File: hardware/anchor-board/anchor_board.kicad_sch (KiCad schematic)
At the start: 54 parts, among them J1 USB4105-GF-A, SW1 SKHHALA010, U1 DWM3001C, U2 TPD2E2U06, U3 BQ24074, U4 DW01A, U5 FS8205A, U6 TLV75530, U7 W25Q128JVSIQ, U8 TPS22916C

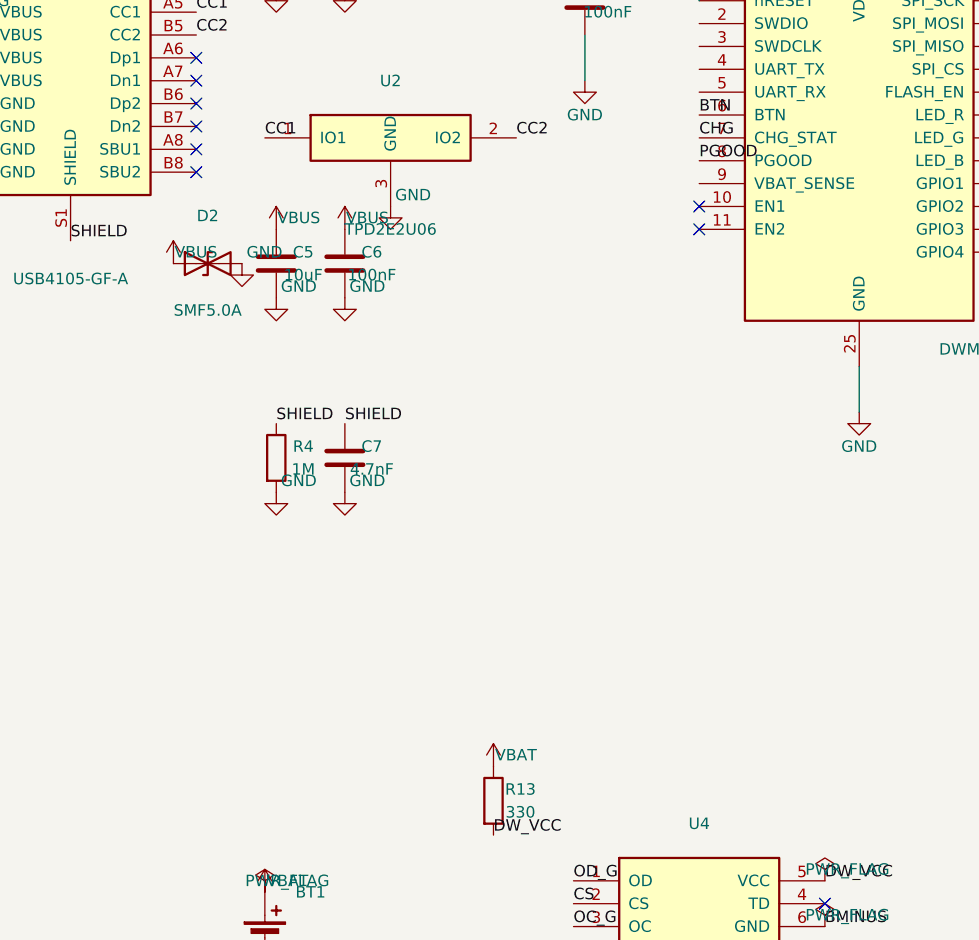
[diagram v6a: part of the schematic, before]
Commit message: Capture §4.8 VBAT voltage sense divider on anchor-board schematic
Adds R22/R23 (1M+1M high-impedance divider) from VBAT with C19 100nF
filter cap, tap driving U1 VBAT_SENSE (pin 9) for the hub's battery_pct
BLE field. ERC 21 -> 19 (remaining errors are §4.9 dev-rail pins).
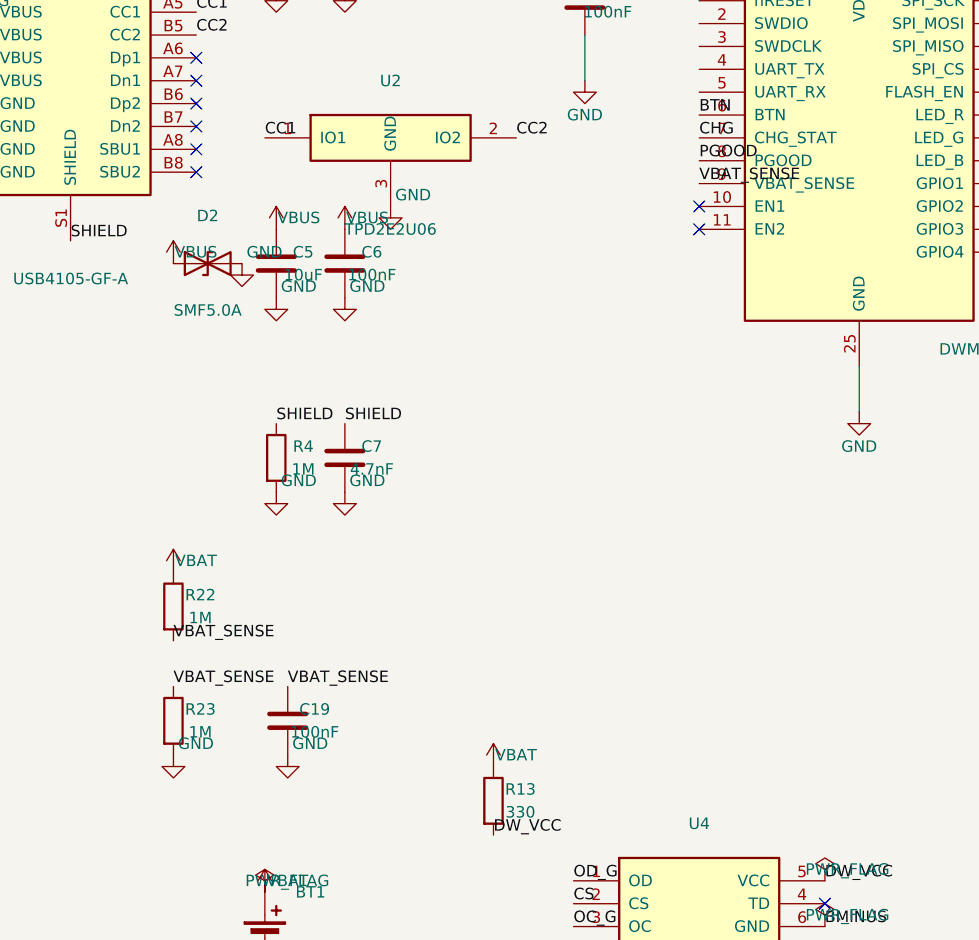
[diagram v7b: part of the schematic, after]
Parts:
- added C19: 100nF, Capacitor_SMD:C_0402_1005Metric, symbol Device:C
- added R22, R23: 1M, Resistor_SMD:R_0402_1005Metric, symbol Device:R
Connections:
- net GND: now also C19.2, R23.2
- net VBAT: now also R22.1
- net VBAT_SENSE: now reaches U1.9 (VBAT_SENSE)
- net VBAT_SENSE: now also C19.1, R22.2, R23.1

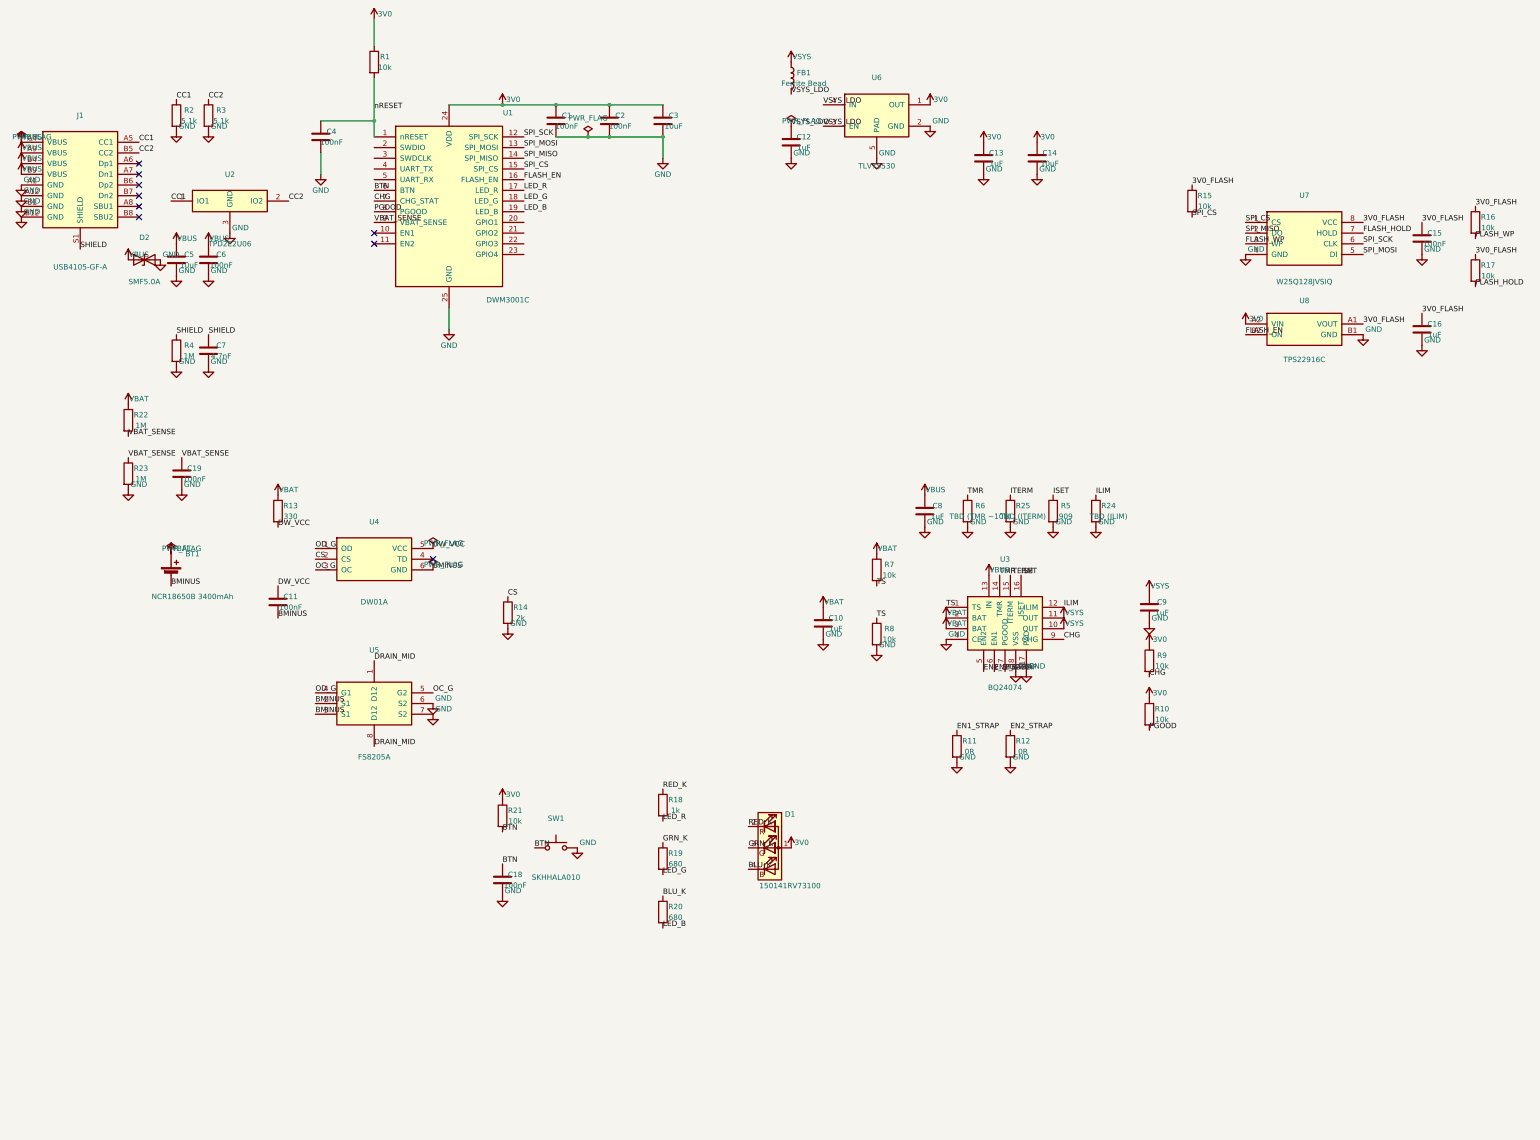
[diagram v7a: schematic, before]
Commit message: Capture §4.9 rail test points + §7 break-off dev rail — schematic ERC-clean
Completes the anchor-board schematic:
- §4.9: TP1-TP6 (VBUS/VSYS/VBAT/3V0/GND x2) + C20 10uF 3V0 bulk cap
- §7 dev rail: J2 2x5 SWD header, J8 Tag-Connect TC2030 pads, J3 UART
  header, J4 GPIO breakout, J5 3V0 current-shunt jumper (+ R26 0R
  production replacement), J6 LED-disable jumper, J7 reset/boot pads
- LDO output split into 3V0_LDO -> (shunt jumper / 0R) -> 3V0 so the
  sleep-current meter sees true load current; LED anode on LED_VCC
  behind the disable jumper
- DWM3001C SWDCLK/UART_RX pins -> passive (driven by external tooling)

ERC: 0 errors, 10 warnings (all footprint-not-found placeholders for
custom parts, resolved at layout).
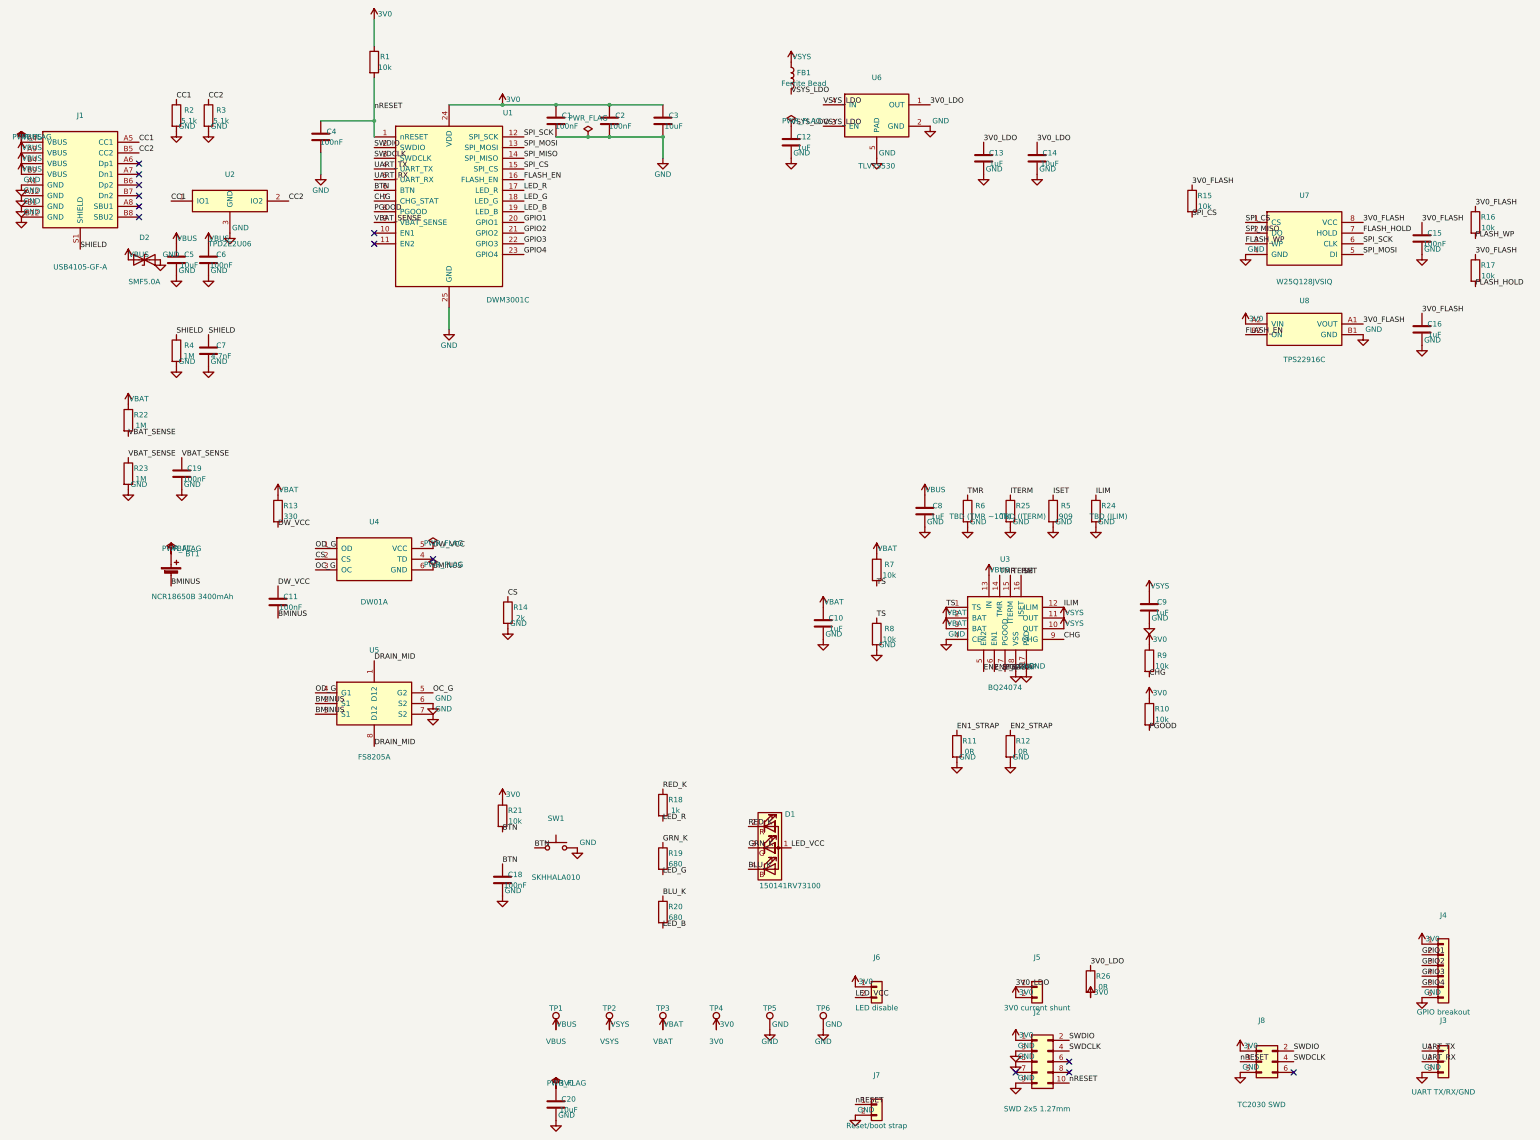
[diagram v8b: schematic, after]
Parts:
- added C20: 10uF, Capacitor_SMD:C_0805_2012Metric, symbol Device:C
- added J2: SWD 2x5 1.27mm, Connector_PinHeader_1.27mm:PinHeader_2x05_P1.27mm_Vertical, symbol Connector_Generic:Conn_02x05_Odd_Even
- added J3: UART TX/RX/GND, Connector_PinHeader_2.54mm:PinHeader_1x03_P2.54mm_Vertical, symbol Connector_Generic:Conn_01x03
- added J4: GPIO breakout, Connector_PinHeader_2.54mm:PinHeader_1x06_P2.54mm_Vertical, symbol Connector_Generic:Conn_01x06
- added J5: 3V0 current shunt, Connector_PinHeader_2.54mm:PinHeader_1x02_P2.54mm_Vertical, symbol Connector_Generic:Conn_01x02
- added J6: LED disable, Connector_PinHeader_2.54mm:PinHeader_1x02_P2.54mm_Vertical, symbol Connector_Generic:Conn_01x02
- added J7: Reset/boot strap, Connector_PinHeader_2.54mm:PinHeader_1x02_P2.54mm_Vertical, symbol Connector_Generic:Conn_01x02
- added J8: TC2030 SWD, infinity-stumps:Tag-Connect_TC2030-IDC-NL, symbol Connector_Generic:Conn_02x03_Odd_Even
- added R26: 0R, Resistor_SMD:R_0402_1005Metric, symbol Device:R
- added TP1: VBUS, TestPoint:TestPoint_Pad_D1.5mm, symbol Connector:TestPoint
- added TP2: VSYS, TestPoint:TestPoint_Pad_D1.5mm, symbol Connector:TestPoint
- added TP3: VBAT, TestPoint:TestPoint_Pad_D1.5mm, symbol Connector:TestPoint
- added TP4: 3V0, TestPoint:TestPoint_Pad_D1.5mm, symbol Connector:TestPoint
- added TP5, TP6: GND, TestPoint:TestPoint_Pad_D1.5mm, symbol Connector:TestPoint
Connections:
- net 3V0: now also C20.1, J2.1 (Pin_1), J4.1 (Pin_1), J5.2 (Pin_2), J6.1 (Pin_1), J8.1 (Pin_1), R26.2, TP4.1; no longer C13.1, C14.1, D1.1 (A), U6.1 (OUT)
- net GND: now also C20.2, J2.3 (Pin_3), J2.5 (Pin_5), J2.9 (Pin_9), J3.3 (Pin_3), J4.6 (Pin_6), J7.2 (Pin_2), J8.5 (Pin_5), TP5.1, TP6.1
- net VBAT: now also TP3.1
- net VBUS: now also TP1.1
- net VSYS: now also TP2.1
- net nRESET: now also J2.10 (Pin_10), J7.1 (Pin_1), J8.3 (Pin_3)
- net SWDIO: now reaches U1.2 (SWDIO)
- net SWDIO: now also J2.2 (Pin_2), J8.2 (Pin_2)
- net GPIO1: now reaches U1.20 (GPIO1)
- net GPIO1: now also J4.2 (Pin_2)
- net GPIO2: now reaches U1.21 (GPIO2)
- net GPIO2: now also J4.3 (Pin_3)
- net GPIO3: now reaches U1.22 (GPIO3)
- net GPIO3: now also J4.4 (Pin_4)
- net GPIO4: now reaches U1.23 (GPIO4)
- net GPIO4: now also J4.5 (Pin_5)
- net SWDCLK: now reaches U1.3 (SWDCLK)
- net SWDCLK: now also J2.4 (Pin_4), J8.4 (Pin_4)
- net UART_TX: now reaches U1.4 (UART_TX)
- net UART_TX: now also J3.1 (Pin_1)
- net UART_RX: now reaches U1.5 (UART_RX)
- net UART_RX: now also J3.2 (Pin_2)
- new net 3V0_LDO: C13.1, C14.1, J5.1 (Pin_1), R26.1, U6.1 (OUT)
- new net LED_VCC: D1.1 (A), J6.2 (Pin_2)
- no-connect marks 9 -> 13
